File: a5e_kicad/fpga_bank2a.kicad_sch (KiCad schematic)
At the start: 2 parts, among them U7 A5EB013B-B23B

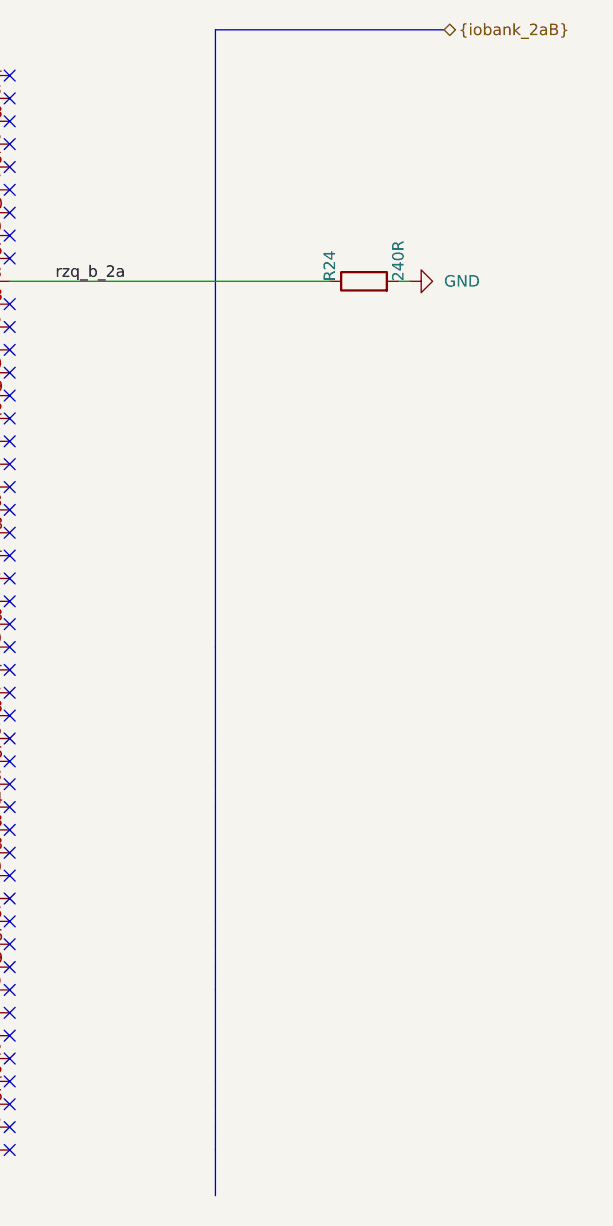
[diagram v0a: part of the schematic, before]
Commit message: Schematic reorg step 9: ERC to zero
- Wires trimmed back to their last label or cap (SDM config lines, LPDDR4
  decoupling rows, PG pins); loose stubs and R29 leftovers removed
- Unused bus links removed: {iob6a}, {iobank_2aB}, {iob6c}, {phy} and the
  io_headers {jtag} (sheet pins, root buses, unnamed internal buses);
  {iob6b} bus tail trimmed

Netdiff: 0 renamed, 0 connectivity diffs. ERC 21 -> 0. PCB unchanged, DRC parity 0.
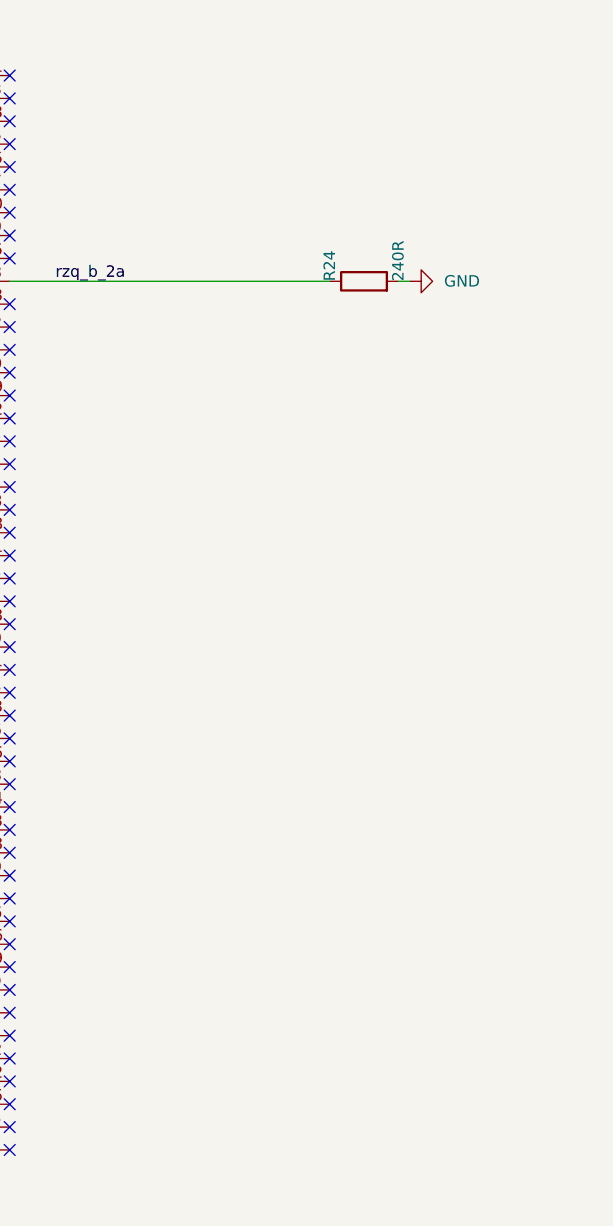
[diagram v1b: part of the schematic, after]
